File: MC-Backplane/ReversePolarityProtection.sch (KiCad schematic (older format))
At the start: 5 parts

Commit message: Add files via upload
updating net names and wires
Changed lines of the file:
@@
 $Descr A4 11693 8268
 encoding utf-8
-Sheet 7 7
+Sheet 2 7
 Title ""
 Date ""
@@
 Wire Wire Line
 	6950 3200 6300 3200
-$Comp
-L power:GND #PWR?
-U 1 1 61FBD2CF
-P 6100 4050
-AR Path="/61FBD2CF" Ref="#PWR?"  Part="1"
-AR Path="/61FBA43E/61FBD2CF" Ref="#PWR?"  Part="1"
-F 0 "#PWR?" H 6100 3800 50  0001 C CNN
-F 1 "GND" H 6105 3877 50  0000 C CNN
-F 2 "" H 6100 4050 50  0001 C CNN
-F 3 "" H 6100 4050 50  0001 C CNN
-	1    6100 4050
-	1    0    0    -1
-$EndComp
 Wire Wire Line
 	6100 3950 6100 4050
@@
 Text Notes 1550 2000 0    50   ~ 0
 RDS of PMOS needs to be really small like miliohms.\n\nDrain current needs to be larger than what the load requires.\nVDS needs to be larger than the source voltage by a significant amount. 24V so around  45V-60V.\n\nThe Zener diode needs a voltage rating of just under VDS of the mosfet. \n\nnot sure about the resistors.
+Text HLabel 6100 4050 0    50   Output ~ 0
+GND
 $EndSCHEMATC

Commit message: beginning layout
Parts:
- removed F?: Fuse, symbol Device:Fuse
- D51: renamed from D?; value Zener BZX84C9V1-7-F -> BZX84C9V1-7-F; footprint (none) -> Package_TO_SOT_SMD:SOT-23_Handsoldering
- U51: renamed from U?; footprint (none) -> Footprints_MC-Backplane:64600001223
- U52: renamed from U?; footprint (none) -> Footprints_MC-Backplane:Vishay_PowerPAK_1212-8_Single
- gave numbers to parts that had none: 1
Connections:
- wire segments 12 -> 10
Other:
- note added: "RDS of PMOS needs to be really small like miliohms.\n\nDrain current needs to be larger than what the load requires.\nVDS needs to be larger than the source voltage by a significant amount. 24V so around 45V-60V.\n\nThe Zener diode needs a voltage rating of just under VDS of the mosfet. \n\n"
- note added: "fuse"
- note added: "zener"
- note removed: "RDS of PMOS needs to be really small like miliohms.\n\nDrain current needs to be larger than what the load requires.\nVDS needs to be larger than the source voltage by a significant amount. 24V so around 45V-60V.\n\nThe Zener diode needs a voltage rating of just under VDS of the mosfet. \n\nnot sure about the resistors."
- note removed: "maybe: 5.5mm barrel jack? \nwith 2.1mm center pole"
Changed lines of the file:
@@
 P 6950 3400
 AR Path="/61FBD2BC" Ref="D?"  Part="1"
-AR Path="/61FBA43E/61FBD2BC" Ref="D?"  Part="1"
-F 0 "D?" V 6904 3480 50  0000 L CNN
-F 1 "Zener BZX84C9V1-7-F" V 6995 3480 50  0000 L CNN
-F 2 "" H 6950 3400 50  0001 C CNN
-F 3 "https://www.digikey.com/en/products/detail/diodes-incorporated/BZX84C9V1-7-F/717755" H 6950 3400 50  0001 C CNN
+AR Path="/61FBA43E/61FBD2BC" Ref="D51"  Part="1"
+F 0 "D51" V 6904 3480 50  0000 L CNN
+F 1 "BZX84C9V1-7-F" V 6995 3480 50  0000 L CNN
+F 2 "Package_TO_SOT_SMD:SOT-23_Handsoldering" H 6950 3400 50  0001 C CNN
+F 3 "https://www.mouser.com/datasheet/2/115/DIOD_S_A0007713711_1-2542835.pdf" H 6950 3400 50  0001 C CNN
 	1    6950 3400
 	0    1    1    0
@@
 P 6100 3850
 AR Path="/61FBD2C2" Ref="R?"  Part="1"
-AR Path="/61FBA43E/61FBD2C2" Ref="R?"  Part="1"
-F 0 "R?" H 6168 3896 50  0000 L CNN
+AR Path="/61FBA43E/61FBD2C2" Ref="R51"  Part="1"
+F 0 "R51" H 6168 3896 50  0000 L CNN
 F 1 "3k" H 6168 3805 50  0000 L CNN
 F 2 "Resistor_SMD:R_1206_3216Metric" H 6100 3850 50  0001 C CNN
@@
 P 5200 3400
 AR Path="/61FBD2D7" Ref="U?"  Part="1"
-AR Path="/61FBA43E/61FBD2D7" Ref="U?"  Part="1"
-F 0 "U?" H 5200 3427 50  0000 C CNN
+AR Path="/61FBA43E/61FBD2D7" Ref="U51"  Part="1"
+F 0 "U51" H 5200 3427 50  0000 C CNN
 F 1 "64600001223" H 5200 3336 50  0000 C CNN
-F 2 "" H 5200 3400 50  0001 C CNN
+F 2 "Footprints_MC-Backplane:64600001223" H 5200 3400 50  0001 C CNN
 F 3 "https://www.littelfuse.com/~/media/electronics/datasheets/fuse_blocks/littelfuse_fuse_block_646_datasheet.pdf.pdf" H 5200 3400 50  0001 C CNN
 	1    5200 3400
@@
 	4500 3200 4800 3200
 $Comp
-L Device:Fuse F?
-U 1 1 61FBD2DF
-P 5200 2700
-AR Path="/61FBD2DF" Ref="F?"  Part="1"
-AR Path="/61FBA43E/61FBD2DF" Ref="F?"  Part="1"
-F 0 "F?" V 5003 2700 50  0000 C CNN
-F 1 "Fuse" V 5094 2700 50  0000 C CNN
-F 2 "" V 5130 2700 50  0001 C CNN
-F 3 "~" H 5200 2700 50  0001 C CNN
-	1    5200 2700
-	0    1    1    0
-$EndComp
-Wire Wire Line
-	5050 2700 5050 2950
-Wire Wire Line
-	5350 2950 5350 2700
-Text Notes 3750 3750 0    50   ~ 0
-maybe:  5.5mm barrel jack? \nwith 2.1mm center pole
-$Comp
 L MC-Backplane:SISS05DN-T1-GE3 U?
 U 1 1 61FBD2E8
 P 6600 3200
 AR Path="/61FBD2E8" Ref="U?"  Part="1"
-AR Path="/61FBA43E/61FBD2E8" Ref="U?"  Part="1"
-F 0 "U?" V 6842 3700 50  0000 C CNN
+AR Path="/61FBA43E/61FBD2E8" Ref="U52"  Part="1"
+F 0 "U52" V 6842 3700 50  0000 C CNN
 F 1 "SISS05DN-T1-GE3" V 6751 3700 50  0000 C CNN
-F 2 "" H 6600 3200 50  0001 C CNN
-F 3 "" H 6600 3200 50  0001 C CNN
+F 2 "Footprints_MC-Backplane:Vishay_PowerPAK_1212-8_Single" H 6600 3200 50  0001 C CNN
+F 3 "https://www.mouser.com/datasheet/2/427/VISH_S_A0010925016_1-2571497.pdf" H 6600 3200 50  0001 C CNN
 	1    6600 3200
 	0    -1   -1   0
@@
 Text HLabel 4500 3200 0    50   Input ~ 0
 24V_unprotected
-Text Notes 1550 2000 0    50   ~ 0
-RDS of PMOS needs to be really small like miliohms.\n\nDrain current needs to be larger than what the load requires.\nVDS needs to be larger than the source voltage by a significant amount. 24V so around  45V-60V.\n\nThe Zener diode needs a voltage rating of just under VDS of the mosfet. \n\nnot sure about the resistors.
+Text Notes 625  1225 0    50   ~ 0
+RDS of PMOS needs to be really small like miliohms.\n\nDrain current needs to be larger than what the load requires.\nVDS needs to be larger than the source voltage by a significant amount. 24V so around  45V-60V.\n\nThe Zener diode needs a voltage rating of just under VDS of the mosfet. \n\n
 Text HLabel 6100 4050 0    50   Output ~ 0
 GND
+Text Notes 7200 3575 0    50   ~ 0
+zener
+Wire Notes Line
+	5050 3000 5050 2775
+Wire Notes Line
+	5050 2775 5325 2775
+Wire Notes Line
+	5325 2775 5325 3000
+Wire Notes Line
+	5125 2700 5125 2800
+Wire Notes Line
+	5125 2800 5250 2800
+Wire Notes Line
+	5250 2800 5250 2700
+Wire Notes Line
+	5250 2700 5125 2700
+Text Notes 5100 2700 0    50   ~ 0
+fuse
 $EndSCHEMATC

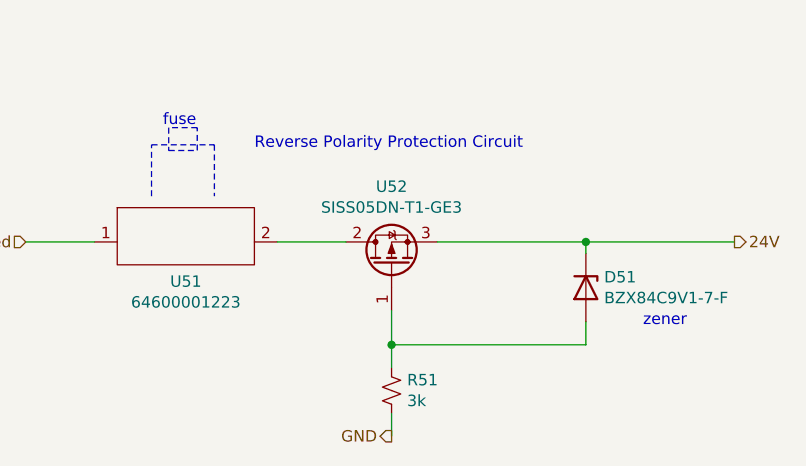
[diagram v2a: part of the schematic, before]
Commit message: schematic reorg and layout begins
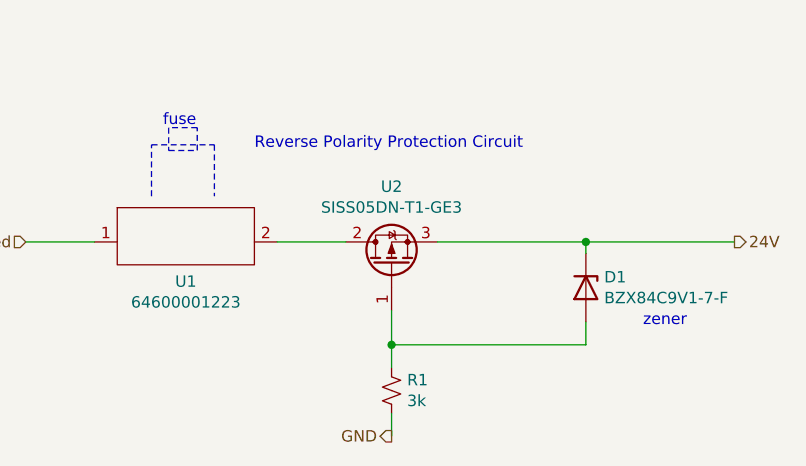
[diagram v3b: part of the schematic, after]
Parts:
- renumbered D51 to D1, R51 to R1, U51 to U1, U52 to U2
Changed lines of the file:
@@
 $Descr A4 11693 8268
 encoding utf-8
-Sheet 2 7
+Sheet 2 14
 Title ""
 Date ""
@@
 P 6950 3400
 AR Path="/61FBD2BC" Ref="D?"  Part="1"
-AR Path="/61FBA43E/61FBD2BC" Ref="D51"  Part="1"
-F 0 "D51" V 6904 3480 50  0000 L CNN
+AR Path="/61FBA43E/61FBD2BC" Ref="D1"  Part="1"
+F 0 "D1" V 6904 3480 50  0000 L CNN
 F 1 "BZX84C9V1-7-F" V 6995 3480 50  0000 L CNN
 F 2 "Package_TO_SOT_SMD:SOT-23_Handsoldering" H 6950 3400 50  0001 C CNN
@@
 P 6100 3850
 AR Path="/61FBD2C2" Ref="R?"  Part="1"
-AR Path="/61FBA43E/61FBD2C2" Ref="R51"  Part="1"
-F 0 "R51" H 6168 3896 50  0000 L CNN
+AR Path="/61FBA43E/61FBD2C2" Ref="R1"  Part="1"
+F 0 "R1" H 6168 3896 50  0000 L CNN
 F 1 "3k" H 6168 3805 50  0000 L CNN
 F 2 "Resistor_SMD:R_1206_3216Metric" H 6100 3850 50  0001 C CNN
@@
 P 5200 3400
 AR Path="/61FBD2D7" Ref="U?"  Part="1"
-AR Path="/61FBA43E/61FBD2D7" Ref="U51"  Part="1"
-F 0 "U51" H 5200 3427 50  0000 C CNN
+AR Path="/61FBA43E/61FBD2D7" Ref="U1"  Part="1"
+F 0 "U1" H 5200 3427 50  0000 C CNN
 F 1 "64600001223" H 5200 3336 50  0000 C CNN
 F 2 "Footprints_MC-Backplane:64600001223" H 5200 3400 50  0001 C CNN
@@
 P 6600 3200
 AR Path="/61FBD2E8" Ref="U?"  Part="1"
-AR Path="/61FBA43E/61FBD2E8" Ref="U52"  Part="1"
-F 0 "U52" V 6842 3700 50  0000 C CNN
+AR Path="/61FBA43E/61FBD2E8" Ref="U2"  Part="1"
+F 0 "U2" V 6842 3700 50  0000 C CNN
 F 1 "SISS05DN-T1-GE3" V 6751 3700 50  0000 C CNN
 F 2 "Footprints_MC-Backplane:Vishay_PowerPAK_1212-8_Single" H 6600 3200 50  0001 C CNN

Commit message: removed some MHs and attempted to fix library
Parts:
- U1: symbol MC-Backplane:64600001223 -> Existing_IC_Models:64600001223
- U2: symbol MC-Backplane:SISS05DN-T1-GE3 -> Existing_IC_Models:SISS05DN-T1-GE3
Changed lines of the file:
@@
 Reverse Polarity Protection Circuit
 $Comp
-L MC-Backplane:64600001223 U?
+L Existing_IC_Models:64600001223 U?
 U 1 1 61FBD2D7
 P 5200 3400
@@
 	4500 3200 4800 3200
 $Comp
-L MC-Backplane:SISS05DN-T1-GE3 U?
+L Existing_IC_Models:SISS05DN-T1-GE3 U?
 U 1 1 61FBD2E8
 P 6600 3200

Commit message: - updated PMOSFET&Zener footprint
reverse polarity protection circuit
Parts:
- D1: symbol Device:D_Zener -> Existing_IC_Models:Zener_diode_3
- U2: symbol Existing_IC_Models:SISS05DN-T1-GE3 -> Existing_IC_Models:PMOS_POWERPAK
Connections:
- net 24V: now also D1.3 (out), U2.1 (S), U2.2 (S); no longer D1.1 (K)
- net at U1.2 (out): now also U2.5 (D); no longer U2.2 (Drain)
- new net: D1.1 (A), R1.1, U2.4 (G)
- now unconnected: D1.2 (A)
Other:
- note added: "there is a correction on this page. Originally the input of zener was parked as pin 2 which does not match the footprint. The output was marked as pin 1 which is actuallt the input.. \n\nTHe PMOS also had issues. The pin numbers did not match the footprint. Ended up with the source connected to 3 different points with the gate and drain attached to numbering."
- moved on the sheet: R1
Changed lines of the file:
@@
 $EndDescr
 $Comp
-L Device:D_Zener D?
+L Existing_IC_Models:Zener_diode_3 D?
 U 1 1 61FBD2BC
-P 6950 3400
+P 6950 3350
 AR Path="/61FBD2BC" Ref="D?"  Part="1"
 AR Path="/61FBA43E/61FBD2BC" Ref="D1"  Part="1"
-F 0 "D1" V 6904 3480 50  0000 L CNN
-F 1 "BZX84C9V1-7-F" V 6995 3480 50  0000 L CNN
-F 2 "Package_TO_SOT_SMD:SOT-23_Handsoldering" H 6950 3400 50  0001 C CNN
-F 3 "https://www.mouser.com/datasheet/2/115/DIOD_S_A0007713711_1-2542835.pdf" H 6950 3400 50  0001 C CNN
-	1    6950 3400
+F 0 "D1" V 6875 3475 50  0000 L CNN
+F 1 "BZX84C9V1-7-F" V 6995 3430 50  0000 L CNN
+F 2 "Package_TO_SOT_SMD:SOT-23_Handsoldering" H 6950 3350 50  0001 C CNN
+F 3 "~" H 6950 3350 50  0001 C CNN
+	1    6950 3350
 	0    1    1    0
 $EndComp
@@
 L Device:R_Small_US R?
 U 1 1 61FBD2C2
-P 6100 3850
+P 6550 3850
 AR Path="/61FBD2C2" Ref="R?"  Part="1"
 AR Path="/61FBA43E/61FBD2C2" Ref="R1"  Part="1"
-F 0 "R1" H 6168 3896 50  0000 L CNN
-F 1 "3k" H 6168 3805 50  0000 L CNN
-F 2 "Resistor_SMD:R_1206_3216Metric" H 6100 3850 50  0001 C CNN
-F 3 "~" H 6100 3850 50  0001 C CNN
-	1    6100 3850
+F 0 "R1" H 6618 3896 50  0000 L CNN
+F 1 "3k" H 6618 3805 50  0000 L CNN
+F 2 "Resistor_SMD:R_1206_3216Metric" H 6550 3850 50  0001 C CNN
+F 3 "~" H 6550 3850 50  0001 C CNN
+	1    6550 3850
 	1    0    0    -1
 $EndComp
 Wire Wire Line
-	6100 3500 6100 3650
+	6950 3500 6950 3650
 Wire Wire Line
-	6950 3550 6950 3650
+	6950 3650 6550 3650
+Connection ~ 6550 3650
 Wire Wire Line
-	6950 3650 6100 3650
-Connection ~ 6100 3650
+	6550 3650 6550 3750
 Wire Wire Line
-	6100 3650 6100 3750
+	6950 3200 6950 3150
 Wire Wire Line
-	6950 3250 6950 3200
-Wire Wire Line
-	6950 3200 6300 3200
-Wire Wire Line
-	6100 3950 6100 4050
+	6550 3950 6550 4050
 Text Notes 5500 2800 0    50   ~ 0
 Reverse Polarity Protection Circuit
@@
 	4500 3200 4800 3200
 $Comp
-L Existing_IC_Models:SISS05DN-T1-GE3 U?
+L Existing_IC_Models:PMOS_POWERPAK U?
 U 1 1 61FBD2E8
-P 6600 3200
+P 6250 3350
 AR Path="/61FBD2E8" Ref="U?"  Part="1"
 AR Path="/61FBA43E/61FBD2E8" Ref="U2"  Part="1"
-F 0 "U2" V 6842 3700 50  0000 C CNN
-F 1 "SISS05DN-T1-GE3" V 6751 3700 50  0000 C CNN
-F 2 "Footprints_MC-Backplane:Vishay_PowerPAK_1212-8_Single" H 6600 3200 50  0001 C CNN
-F 3 "https://www.mouser.com/datasheet/2/427/VISH_S_A0010925016_1-2571497.pdf" H 6600 3200 50  0001 C CNN
-	1    6600 3200
-	0    -1   -1   0
+F 0 "U2" H 6250 3850 50  0000 C CNN
+F 1 "SISS05DN-T1-GE3" H 6275 3750 50  0000 C CNN
+F 2 "Footprints_MC-Backplane:Vishay_PowerPAK_1212-8_Single" H 6250 3350 50  0001 C CNN
+F 3 "https://www.mouser.com/datasheet/2/427/VISH_S_A0010925016_1-2571497.pdf" H 6250 3350 50  0001 C CNN
+	1    6250 3350
+	-1   0    0    -1
 $EndComp
 Wire Wire Line
-	6950 3200 7600 3200
-Connection ~ 6950 3200
-Text HLabel 7600 3200 2    50   Output ~ 0
+	6950 3150 7600 3150
+Connection ~ 6950 3150
+Text HLabel 7600 3150 2    50   Output ~ 0
 24V
 Text HLabel 4500 3200 0    50   Input ~ 0
@@
 Text Notes 625  1225 0    50   ~ 0
 RDS of PMOS needs to be really small like miliohms.\n\nDrain current needs to be larger than what the load requires.\nVDS needs to be larger than the source voltage by a significant amount. 24V so around  45V-60V.\n\nThe Zener diode needs a voltage rating of just under VDS of the mosfet. \n\n
-Text HLabel 6100 4050 0    50   Output ~ 0
+Text HLabel 6550 4050 0    50   Output ~ 0
 GND
 Text Notes 7200 3575 0    50   ~ 0
@@
 Text Notes 5100 2700 0    50   ~ 0
 fuse
+Wire Wire Line
+	6550 3350 6550 3650
+Wire Wire Line
+	6550 3050 6625 3050
+Wire Wire Line
+	6625 3150 6950 3150
+Wire Wire Line
+	6550 3250 6625 3250
+Wire Wire Line
+	6625 3250 6625 3150
+Connection ~ 6625 3150
+Wire Wire Line
+	6550 3150 6625 3150
+Wire Wire Line
+	6625 3050 6625 3150
+Text Notes 3550 1750 0    50   ~ 0
+there is a correction on this page. Originally the input of zener was parked as pin 2 which does not match the footprint. The output was marked as pin 1 which is actuallt the input..  \n\nTHe PMOS also had issues. The pin numbers did not match the footprint. Ended up with the source connected to 3 different points with the gate and drain attached to numbering.
 $EndSCHEMATC

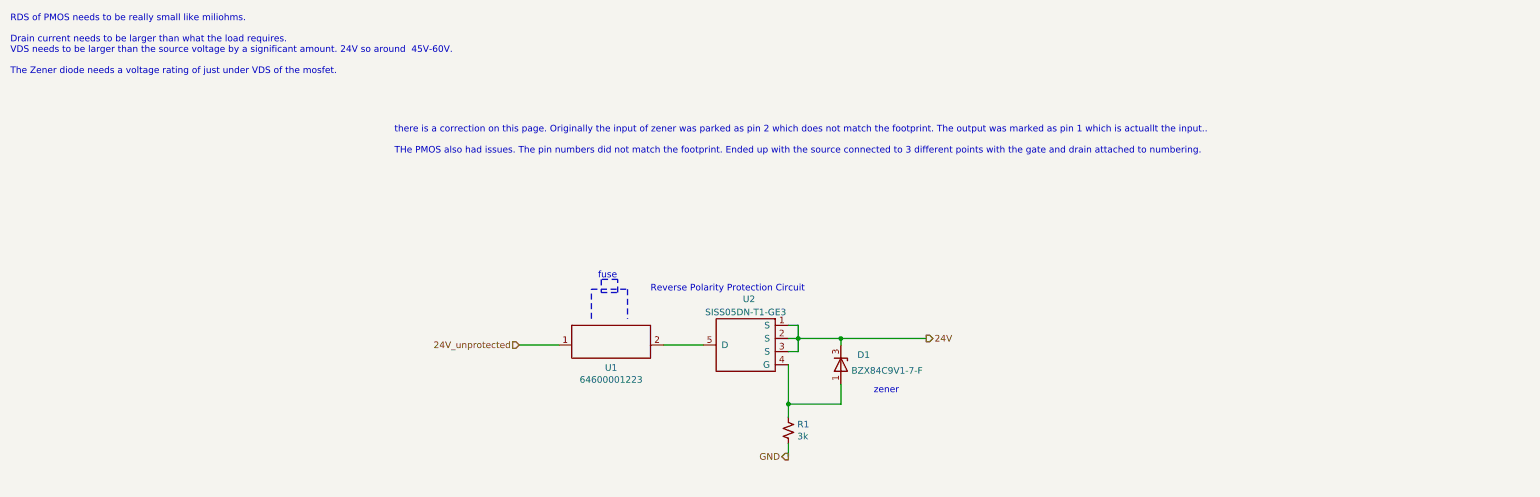
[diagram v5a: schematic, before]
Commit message: increased 24V trace width.
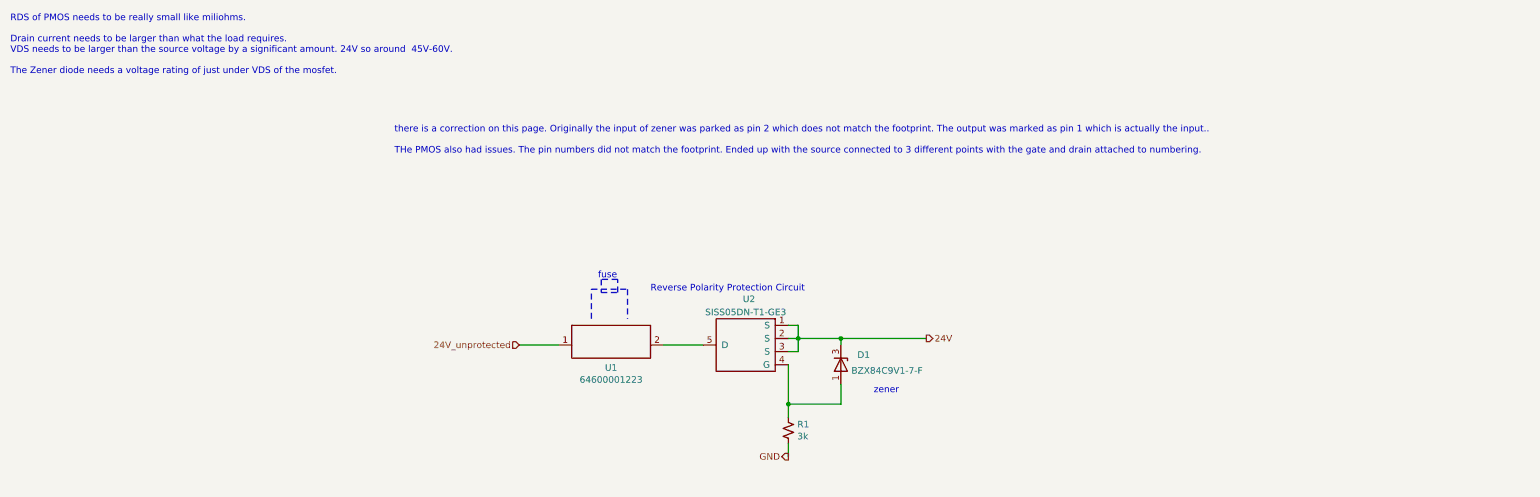
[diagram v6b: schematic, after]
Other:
- note added: "there is a correction on this page. Originally the input of zener was parked as pin 2 which does not match the footprint. The output was marked as pin 1 which is actually the input.. \n\nTHe PMOS also had issues. The pin numbers did not match the footprint. Ended up with the source connected to 3 different points with the gate and drain attached to numbering."
- note removed: "there is a correction on this page. Originally the input of zener was parked as pin 2 which does not match the footprint. The output was marked as pin 1 which is actuallt the input.. \n\nTHe PMOS also had issues. The pin numbers did not match the footprint. Ended up with the source connected to 3 different points with the gate and drain attached to numbering."
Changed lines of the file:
@@
 	6625 3050 6625 3150
 Text Notes 3550 1750 0    50   ~ 0
-there is a correction on this page. Originally the input of zener was parked as pin 2 which does not match the footprint. The output was marked as pin 1 which is actuallt the input..  \n\nTHe PMOS also had issues. The pin numbers did not match the footprint. Ended up with the source connected to 3 different points with the gate and drain attached to numbering.
+there is a correction on this page. Originally the input of zener was parked as pin 2 which does not match the footprint. The output was marked as pin 1 which is actually the input..  \n\nTHe PMOS also had issues. The pin numbers did not match the footprint. Ended up with the source connected to 3 different points with the gate and drain attached to numbering.
 $EndSCHEMATC
